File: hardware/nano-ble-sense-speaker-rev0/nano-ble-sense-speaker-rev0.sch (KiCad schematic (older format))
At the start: 1 part, among them J1 Arduino-NANO-33

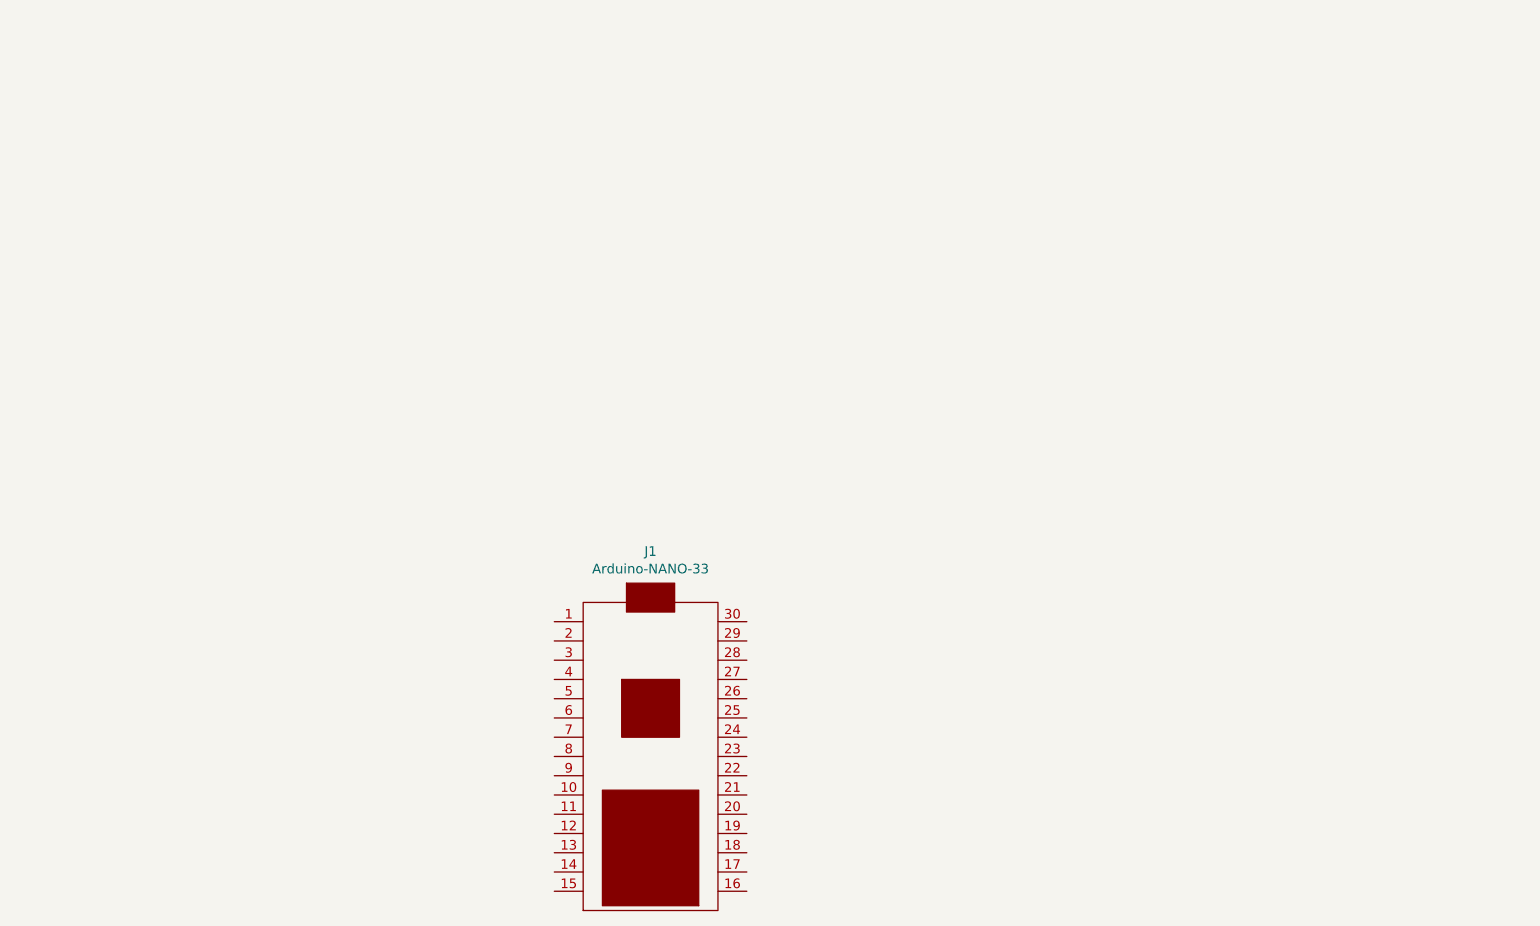
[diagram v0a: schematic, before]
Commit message: Make first PCB design
PCB Design in KiCAD now has:
- OLED 1.3inch
- power supply using LM7805 and capacitors

TODO:
- Add I2S module either as the breakout board of on the PCB as an SMD
comp.
- Move components a little more closer.
- Add PCB ground pad, and make paths between all components.
- Add pull up resistors to the OLED I2C pins

Signed-off-by: Dhruva Gole <goledhruva@gmail.com>
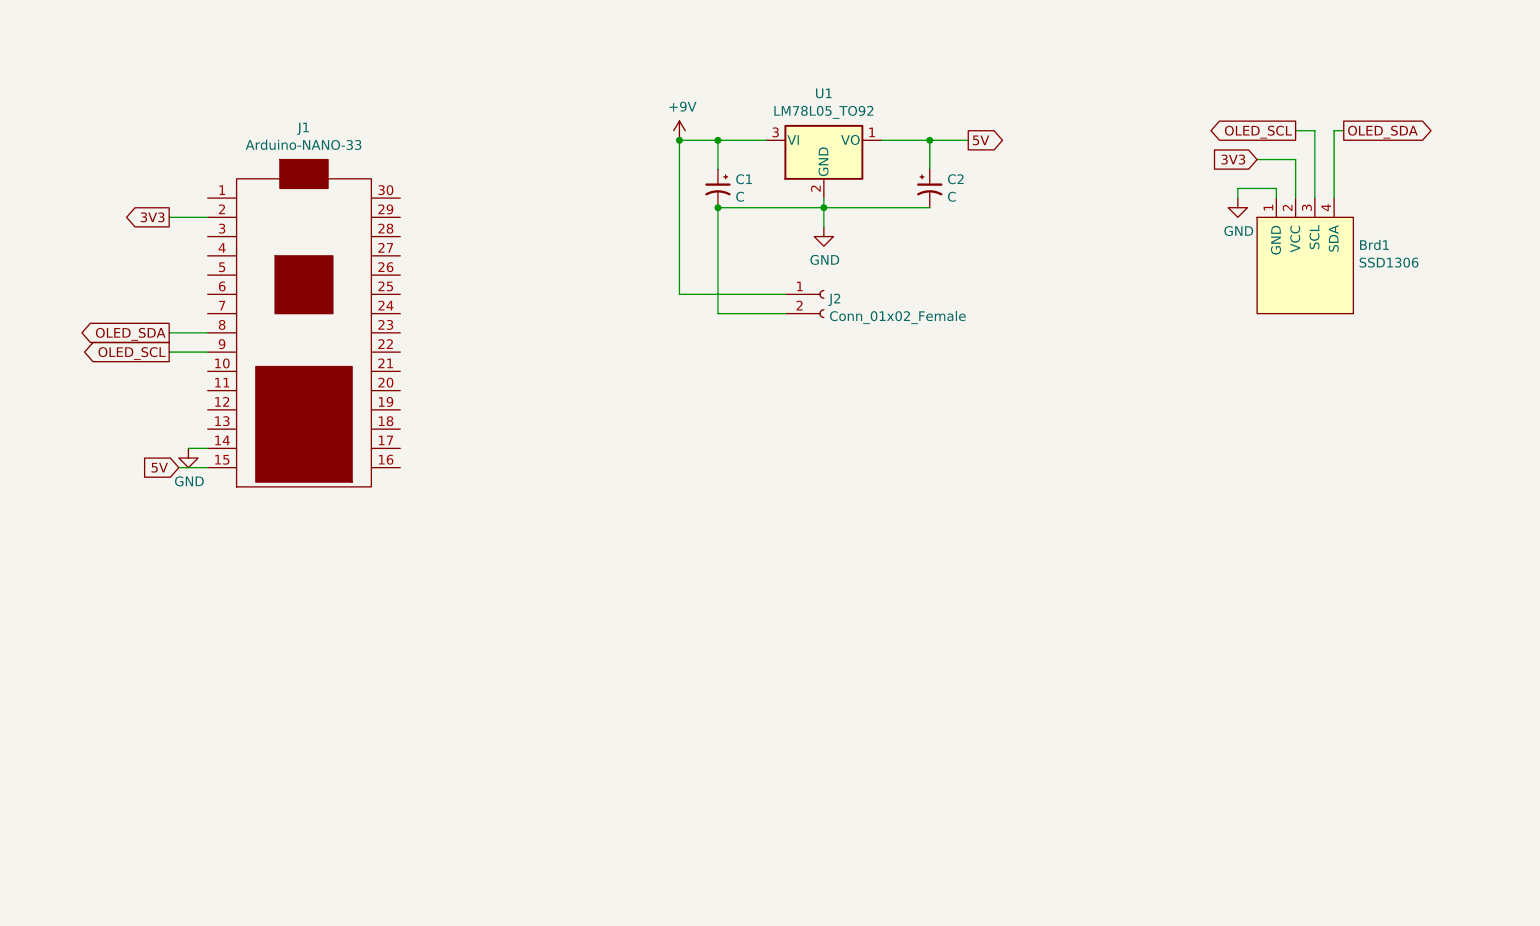
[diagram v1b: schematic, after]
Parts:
- added Brd1: SSD1306, SSD1306:128x64OLED, symbol SSD1306-128x64_OLED:SSD1306
- added C1, C2: C, Capacitor_THT:CP_Radial_D6.3mm_P2.50mm, symbol Device:CP1_Small
- added J2: Conn_01x02_Female, Connector_PinSocket_2.54mm:PinSocket_1x02_P2.54mm_Vertical, symbol Connector:Conn_01x02_Female
- added U1: LM78L05_TO92, Package_TO_SOT_THT:TO-220-3_Vertical, symbol Linear-reg:LM78L05_TO92
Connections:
- net GND: now reaches J1.14
- net GND: now also Brd1.1 (GND), C1.2, C2.2, J2.2 (Pin_2), U1.2 (GND)
- net 5V: now reaches J1.15
- net 5V: now also C2.1, U1.1 (VO)
- net 3V3: now reaches J1.2
- net 3V3: now also Brd1.2 (VCC)
- net OLED_SDA: now reaches J1.8
- net OLED_SDA: now also Brd1.4 (SDA)
- net OLED_SCL: now reaches J1.9
- net OLED_SCL: now also Brd1.3 (SCL)
- new net +9V: C1.1, J2.1 (Pin_1), U1.3 (VI)
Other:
- moved on the sheet: J1
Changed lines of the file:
@@
 L Arduino-nano-33:Arduino-NANO-33 J1
 U 1 1 6140B0DA
-P 3850 4300
-F 0 "J1" H 3850 5365 50  0000 C CNN
-F 1 "Arduino-NANO-33" H 3850 5274 50  0000 C CNN
-F 2 "Nano_33:NANO_33_Socket_Castell" H 3525 4200 50  0001 C CNN
-F 3 "~" H 3525 4200 50  0001 C CNN
-	1    3850 4300
+P 2050 2100
+F 0 "J1" H 2050 3165 50  0000 C CNN
+F 1 "Arduino-NANO-33" H 2050 3074 50  0000 C CNN
+F 2 "Nano_33:NANO_33_Socket_Castell" H 1725 2000 50  0001 C CNN
+F 3 "~" H 1725 2000 50  0001 C CNN
+	1    2050 2100
 	1    0    0    -1
 $EndComp
+Text GLabel 1400 2800 0    50   Input ~ 0
+5V
+Wire Wire Line
+	1400 2800 1550 2800
+Text GLabel 5500 1100 2    50   Output ~ 0
+5V
+$Comp
+L power:GND #PWR0101
+U 1 1 616D7A98
+P 4750 1550
+F 0 "#PWR0101" H 4750 1300 50  0001 C CNN
+F 1 "GND" H 4755 1377 50  0000 C CNN
+F 2 "" H 4750 1550 50  0001 C CNN
+F 3 "" H 4750 1550 50  0001 C CNN
+	1    4750 1550
+	1    0    0    -1
+$EndComp
+$Comp
+L power:GND #PWR0102
+U 1 1 616D7EA0
+P 1450 2700
+F 0 "#PWR0102" H 1450 2450 50  0001 C CNN
+F 1 "GND" H 1455 2527 50  0000 C CNN
+F 2 "" H 1450 2700 50  0001 C CNN
+F 3 "" H 1450 2700 50  0001 C CNN
+	1    1450 2700
+	1    0    0    -1
+$EndComp
+Wire Wire Line
+	1450 2700 1550 2700
+Wire Wire Line
+	4750 1400 4750 1450
+$Comp
+L Linear-reg:LM78L05_TO92 U1
+U 1 1 616D28C0
+P 4750 1100
+F 0 "U1" H 4750 1342 50  0000 C CNN
+F 1 "LM78L05_TO92" H 4750 1251 50  0000 C CNN
+F 2 "Package_TO_SOT_THT:TO-220-3_Vertical" H 4750 1325 50  0001 C CIN
+F 3 "https://www.onsemi.com/pub/Collateral/MC78L06A-D.pdf" H 4750 1050 50  0001 C CNN
+	1    4750 1100
+	1    0    0    -1
+$EndComp
+$Comp
+L Device:CP1_Small C2
+U 1 1 616F6CCF
+P 5300 1350
+F 0 "C2" H 5391 1396 50  0000 L CNN
+F 1 "C" H 5391 1305 50  0000 L CNN
+F 2 "Capacitor_THT:CP_Radial_D6.3mm_P2.50mm" H 5300 1350 50  0001 C CNN
+F 3 "~" H 5300 1350 50  0001 C CNN
+	1    5300 1350
+	1    0    0    -1
+$EndComp
+$Comp
+L Device:CP1_Small C1
+U 1 1 616FACC5
+P 4200 1350
+F 0 "C1" H 4109 1396 50  0000 R CNN
+F 1 "C" H 4109 1305 50  0000 R CNN
+F 2 "Capacitor_THT:CP_Radial_D6.3mm_P2.50mm" H 4200 1350 50  0001 C CNN
+F 3 "~" H 4200 1350 50  0001 C CNN
+	1    4200 1350
+	-1   0    0    -1
+$EndComp
+Wire Wire Line
+	5050 1100 5300 1100
+Wire Wire Line
+	5300 1250 5300 1100
+Connection ~ 5300 1100
+Wire Wire Line
+	5300 1100 5500 1100
+Wire Wire Line
+	4200 1250 4200 1100
+Wire Wire Line
+	4200 1100 4450 1100
+Wire Wire Line
+	4200 1450 4750 1450
+Connection ~ 4750 1450
+Wire Wire Line
+	4750 1450 4750 1550
+Wire Wire Line
+	5300 1450 4750 1450
+$Comp
+L power:+9V #PWR0103
+U 1 1 61703537
+P 4000 1100
+F 0 "#PWR0103" H 4000 950 50  0001 C CNN
+F 1 "+9V" H 4015 1273 50  0000 C CNN
+F 2 "" H 4000 1100 50  0001 C CNN
+F 3 "" H 4000 1100 50  0001 C CNN
+	1    4000 1100
+	1    0    0    -1
+$EndComp
+Wire Wire Line
+	4000 1100 4200 1100
+Connection ~ 4200 1100
+$Comp
+L Connector:Conn_01x02_Female J2
+U 1 1 6170C5E3
+P 4750 1900
+F 0 "J2" H 4778 1876 50  0000 L CNN
+F 1 "Conn_01x02_Female" H 4778 1785 50  0000 L CNN
+F 2 "Connector_PinSocket_2.54mm:PinSocket_1x02_P2.54mm_Vertical" H 4750 1900 50  0001 C CNN
+F 3 "~" H 4750 1900 50  0001 C CNN
+	1    4750 1900
+	1    0    0    -1
+$EndComp
+Wire Wire Line
+	4000 1100 4000 1900
+Wire Wire Line
+	4000 1900 4550 1900
+Connection ~ 4000 1100
+Wire Wire Line
+	4200 1450 4200 2000
+Wire Wire Line
+	4200 2000 4550 2000
+Connection ~ 4200 1450
+$Comp
+L SSD1306-128x64_OLED:SSD1306 Brd1
+U 1 1 61713D71
+P 7250 1750
+F 0 "Brd1" H 7528 1854 50  0000 L CNN
+F 1 "SSD1306" H 7528 1763 50  0000 L CNN
+F 2 "SSD1306:128x64OLED" H 7250 2000 50  0001 C CNN
+F 3 "" H 7250 2000 50  0001 C CNN
+	1    7250 1750
+	1    0    0    -1
+$EndComp
+Text GLabel 1350 1500 0    50   Output ~ 0
+3V3
+Text GLabel 7000 1200 0    50   Input ~ 0
+3V3
+$Comp
+L power:GND #PWR0104
+U 1 1 61718B31
+P 6900 1400
+F 0 "#PWR0104" H 6900 1150 50  0001 C CNN
+F 1 "GND" H 6905 1227 50  0000 C CNN
+F 2 "" H 6900 1400 50  0001 C CNN
+F 3 "" H 6900 1400 50  0001 C CNN
+	1    6900 1400
+	1    0    0    -1
+$EndComp
+Wire Wire Line
+	6900 1400 6900 1350
+Wire Wire Line
+	6900 1350 7100 1350
+Wire Wire Line
+	7100 1350 7100 1400
+Wire Wire Line
+	7200 1200 7200 1400
+Wire Wire Line
+	7200 1200 7000 1200
+Text GLabel 7200 1050 0    50   Output ~ 0
+OLED_SCL
+Text GLabel 7450 1050 2    50   Output ~ 0
+OLED_SDA
+Wire Wire Line
+	7200 1050 7300 1050
+Wire Wire Line
+	7300 1050 7300 1400
+Wire Wire Line
+	7400 1400 7400 1050
+Wire Wire Line
+	7400 1050 7450 1050
+Text GLabel 1350 2100 0    50   Output ~ 0
+OLED_SDA
+Text GLabel 1350 2200 0    50   Output ~ 0
+OLED_SCL
+Wire Wire Line
+	1350 2100 1550 2100
+Wire Wire Line
+	1350 2200 1550 2200
+Wire Wire Line
+	1350 1500 1550 1500
 $EndSCHEMATC

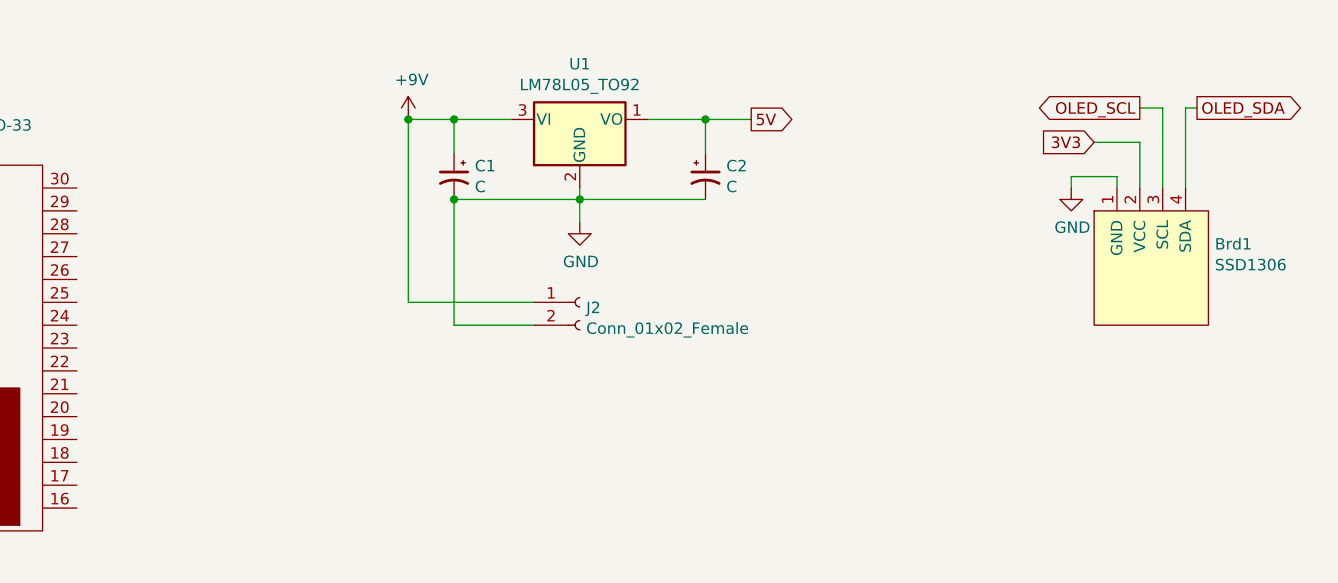
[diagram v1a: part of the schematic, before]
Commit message: Add pull up resistors to I2C
Signed-off-by: Dhruva Gole <goledhruva@gmail.com>
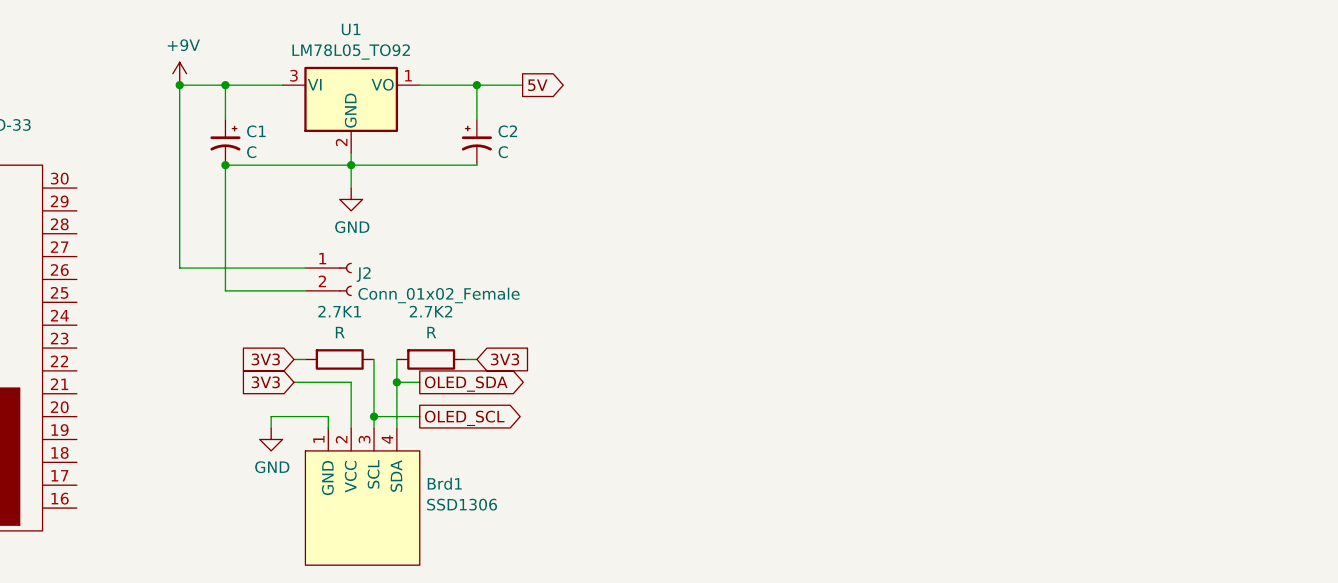
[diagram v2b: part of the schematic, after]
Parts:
- added 2.7K1, 2.7K2: R, Resistor_SMD:R_0603_1608Metric_Pad0.98x0.95mm_HandSolder, symbol Device:R
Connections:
- net 3V3: now also 2.7K1.2, 2.7K2.1
- net OLED_SCL: now also 2.7K1.1
- net OLED_SDA: now also 2.7K2.2
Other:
- moved on the sheet: Brd1, C1, C2, J2, U1
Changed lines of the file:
@@
 Wire Wire Line
 	1400 2800 1550 2800
-Text GLabel 5500 1100 2    50   Output ~ 0
+Text GLabel 4500 950  2    50   Output ~ 0
 5V
 $Comp
 L power:GND #PWR0101
 U 1 1 616D7A98
-P 4750 1550
-F 0 "#PWR0101" H 4750 1300 50  0001 C CNN
-F 1 "GND" H 4755 1377 50  0000 C CNN
-F 2 "" H 4750 1550 50  0001 C CNN
-F 3 "" H 4750 1550 50  0001 C CNN
-	1    4750 1550
+P 3750 1400
+F 0 "#PWR0101" H 3750 1150 50  0001 C CNN
+F 1 "GND" H 3755 1227 50  0000 C CNN
+F 2 "" H 3750 1400 50  0001 C CNN
+F 3 "" H 3750 1400 50  0001 C CNN
+	1    3750 1400
 	1    0    0    -1
 $EndComp
@@
 	1450 2700 1550 2700
 Wire Wire Line
-	4750 1400 4750 1450
+	3750 1250 3750 1300
 $Comp
 L Linear-reg:LM78L05_TO92 U1
 U 1 1 616D28C0
-P 4750 1100
-F 0 "U1" H 4750 1342 50  0000 C CNN
-F 1 "LM78L05_TO92" H 4750 1251 50  0000 C CNN
-F 2 "Package_TO_SOT_THT:TO-220-3_Vertical" H 4750 1325 50  0001 C CIN
-F 3 "https://www.onsemi.com/pub/Collateral/MC78L06A-D.pdf" H 4750 1050 50  0001 C CNN
-	1    4750 1100
+P 3750 950
+F 0 "U1" H 3750 1192 50  0000 C CNN
+F 1 "LM78L05_TO92" H 3750 1101 50  0000 C CNN
+F 2 "Package_TO_SOT_THT:TO-220-3_Vertical" H 3750 1175 50  0001 C CIN
+F 3 "https://www.onsemi.com/pub/Collateral/MC78L06A-D.pdf" H 3750 900 50  0001 C CNN
+	1    3750 950
 	1    0    0    -1
 $EndComp
@@
 L Device:CP1_Small C2
 U 1 1 616F6CCF
-P 5300 1350
-F 0 "C2" H 5391 1396 50  0000 L CNN
-F 1 "C" H 5391 1305 50  0000 L CNN
-F 2 "Capacitor_THT:CP_Radial_D6.3mm_P2.50mm" H 5300 1350 50  0001 C CNN
-F 3 "~" H 5300 1350 50  0001 C CNN
-	1    5300 1350
+P 4300 1200
+F 0 "C2" H 4391 1246 50  0000 L CNN
+F 1 "C" H 4391 1155 50  0000 L CNN
+F 2 "Capacitor_THT:CP_Radial_D6.3mm_P2.50mm" H 4300 1200 50  0001 C CNN
+F 3 "~" H 4300 1200 50  0001 C CNN
+	1    4300 1200
 	1    0    0    -1
 $EndComp
@@
 L Device:CP1_Small C1
 U 1 1 616FACC5
-P 4200 1350
-F 0 "C1" H 4109 1396 50  0000 R CNN
-F 1 "C" H 4109 1305 50  0000 R CNN
-F 2 "Capacitor_THT:CP_Radial_D6.3mm_P2.50mm" H 4200 1350 50  0001 C CNN
-F 3 "~" H 4200 1350 50  0001 C CNN
-	1    4200 1350
+P 3200 1200
+F 0 "C1" H 3109 1246 50  0000 R CNN
+F 1 "C" H 3109 1155 50  0000 R CNN
+F 2 "Capacitor_THT:CP_Radial_D6.3mm_P2.50mm" H 3200 1200 50  0001 C CNN
+F 3 "~" H 3200 1200 50  0001 C CNN
+	1    3200 1200
 	-1   0    0    -1
 $EndComp
 Wire Wire Line
-	5050 1100 5300 1100
-Wire Wire Line
-	5300 1250 5300 1100
-Connection ~ 5300 1100
-Wire Wire Line
-	5300 1100 5500 1100
-Wire Wire Line
-	4200 1250 4200 1100
-Wire Wire Line
-	4200 1100 4450 1100
-Wire Wire Line
-	4200 1450 4750 1450
-Connection ~ 4750 1450
-Wire Wire Line
-	4750 1450 4750 1550
-Wire Wire Line
-	5300 1450 4750 1450
+	4050 950  4300 950
+Wire Wire Line
+	4300 1100 4300 950
+Connection ~ 4300 950
+Wire Wire Line
+	4300 950  4500 950
+Wire Wire Line
+	3200 1100 3200 950
+Wire Wire Line
+	3200 950  3450 950
+Wire Wire Line
+	3200 1300 3750 1300
+Connection ~ 3750 1300
+Wire Wire Line
+	3750 1300 3750 1400
+Wire Wire Line
+	4300 1300 3750 1300
 $Comp
 L power:+9V #PWR0103
 U 1 1 61703537
-P 4000 1100
-F 0 "#PWR0103" H 4000 950 50  0001 C CNN
-F 1 "+9V" H 4015 1273 50  0000 C CNN
-F 2 "" H 4000 1100 50  0001 C CNN
-F 3 "" H 4000 1100 50  0001 C CNN
-	1    4000 1100
-	1    0    0    -1
-$EndComp
-Wire Wire Line
-	4000 1100 4200 1100
-Connection ~ 4200 1100
+P 3000 950
+F 0 "#PWR0103" H 3000 800 50  0001 C CNN
+F 1 "+9V" H 3015 1123 50  0000 C CNN
+F 2 "" H 3000 950 50  0001 C CNN
+F 3 "" H 3000 950 50  0001 C CNN
+	1    3000 950
+	1    0    0    -1
+$EndComp
+Wire Wire Line
+	3000 950  3200 950
+Connection ~ 3200 950
 $Comp
 L Connector:Conn_01x02_Female J2
 U 1 1 6170C5E3
-P 4750 1900
-F 0 "J2" H 4778 1876 50  0000 L CNN
-F 1 "Conn_01x02_Female" H 4778 1785 50  0000 L CNN
-F 2 "Connector_PinSocket_2.54mm:PinSocket_1x02_P2.54mm_Vertical" H 4750 1900 50  0001 C CNN
-F 3 "~" H 4750 1900 50  0001 C CNN
-	1    4750 1900
-	1    0    0    -1
-$EndComp
-Wire Wire Line
-	4000 1100 4000 1900
-Wire Wire Line
-	4000 1900 4550 1900
-Connection ~ 4000 1100
-Wire Wire Line
-	4200 1450 4200 2000
-Wire Wire Line
-	4200 2000 4550 2000
-Connection ~ 4200 1450
+P 3750 1750
+F 0 "J2" H 3778 1726 50  0000 L CNN
+F 1 "Conn_01x02_Female" H 3778 1635 50  0000 L CNN
+F 2 "Connector_PinSocket_2.54mm:PinSocket_1x02_P2.54mm_Vertical" H 3750 1750 50  0001 C CNN
+F 3 "~" H 3750 1750 50  0001 C CNN
+	1    3750 1750
+	1    0    0    -1
+$EndComp
+Wire Wire Line
+	3000 950  3000 1750
+Wire Wire Line
+	3000 1750 3550 1750
+Connection ~ 3000 950
+Wire Wire Line
+	3200 1300 3200 1850
+Wire Wire Line
+	3200 1850 3550 1850
+Connection ~ 3200 1300
 $Comp
 L SSD1306-128x64_OLED:SSD1306 Brd1
 U 1 1 61713D71
-P 7250 1750
-F 0 "Brd1" H 7528 1854 50  0000 L CNN
-F 1 "SSD1306" H 7528 1763 50  0000 L CNN
-F 2 "SSD1306:128x64OLED" H 7250 2000 50  0001 C CNN
-F 3 "" H 7250 2000 50  0001 C CNN
-	1    7250 1750
+P 3800 2800
+F 0 "Brd1" H 4078 2904 50  0000 L CNN
+F 1 "SSD1306" H 4078 2813 50  0000 L CNN
+F 2 "SSD1306:128x64OLED" H 3800 3050 50  0001 C CNN
+F 3 "" H 3800 3050 50  0001 C CNN
+	1    3800 2800
 	1    0    0    -1
 $EndComp
 Text GLabel 1350 1500 0    50   Output ~ 0
 3V3
-Text GLabel 7000 1200 0    50   Input ~ 0
+Text GLabel 3500 2250 0    50   Input ~ 0
 3V3
 $Comp
 L power:GND #PWR0104
 U 1 1 61718B31
-P 6900 1400
-F 0 "#PWR0104" H 6900 1150 50  0001 C CNN
-F 1 "GND" H 6905 1227 50  0000 C CNN
-F 2 "" H 6900 1400 50  0001 C CNN
-F 3 "" H 6900 1400 50  0001 C CNN
-	1    6900 1400
-	1    0    0    -1
-$EndComp
-Wire Wire Line
-	6900 1400 6900 1350
-Wire Wire Line
-	6900 1350 7100 1350
-Wire Wire Line
-	7100 1350 7100 1400
-Wire Wire Line
-	7200 1200 7200 1400
-Wire Wire Line
-	7200 1200 7000 1200
-Text GLabel 7200 1050 0    50   Output ~ 0
+P 3400 2450
+F 0 "#PWR0104" H 3400 2200 50  0001 C CNN
+F 1 "GND" H 3405 2277 50  0000 C CNN
+F 2 "" H 3400 2450 50  0001 C CNN
+F 3 "" H 3400 2450 50  0001 C CNN
+	1    3400 2450
+	1    0    0    -1
+$EndComp
+Wire Wire Line
+	3650 2400 3650 2450
+Wire Wire Line
+	3750 2250 3750 2450
+Text GLabel 4050 2400 2    50   Output ~ 0
 OLED_SCL
-Text GLabel 7450 1050 2    50   Output ~ 0
+Text GLabel 4050 2250 2    50   Output ~ 0
 OLED_SDA
-Wire Wire Line
-	7200 1050 7300 1050
-Wire Wire Line
-	7300 1050 7300 1400
-Wire Wire Line
-	7400 1400 7400 1050
-Wire Wire Line
-	7400 1050 7450 1050
 Text GLabel 1350 2100 0    50   Output ~ 0
 OLED_SDA
@@
 Wire Wire Line
 	1350 1500 1550 1500
+$Comp
+L Device:R 2.7K2
+U 1 1 616C6DBD
+P 4100 2150
+F 0 "2.7K2" V 3893 2150 50  0000 C CNN
+F 1 "R" V 3984 2150 50  0000 C CNN
+F 2 "Resistor_SMD:R_0603_1608Metric_Pad0.98x0.95mm_HandSolder" V 4030 2150 50  0001 C CNN
+F 3 "~" H 4100 2150 50  0001 C CNN
+	1    4100 2150
+	0    1    1    0
+$EndComp
+$Comp
+L Device:R 2.7K1
+U 1 1 616C707B
+P 3700 2150
+F 0 "2.7K1" V 3493 2150 50  0000 C CNN
+F 1 "R" V 3584 2150 50  0000 C CNN
+F 2 "Resistor_SMD:R_0603_1608Metric_Pad0.98x0.95mm_HandSolder" V 3630 2150 50  0001 C CNN
+F 3 "~" H 3700 2150 50  0001 C CNN
+	1    3700 2150
+	0    1    1    0
+$EndComp
+Text GLabel 4300 2150 2    50   Input ~ 0
+3V3
+Text GLabel 3500 2150 0    50   Input ~ 0
+3V3
+Wire Wire Line
+	3400 2400 3400 2450
+Wire Wire Line
+	3400 2400 3650 2400
+Wire Wire Line
+	3500 2250 3750 2250
+Wire Wire Line
+	3500 2150 3550 2150
+Wire Wire Line
+	3850 2450 3850 2400
+Wire Wire Line
+	4050 2250 3950 2250
+Wire Wire Line
+	4050 2400 3850 2400
+Connection ~ 3850 2400
+Wire Wire Line
+	3850 2400 3850 2150
+Wire Wire Line
+	3950 2450 3950 2250
+Wire Wire Line
+	4250 2150 4300 2150
+Wire Wire Line
+	3950 2150 3950 2250
+Connection ~ 3950 2250
 $EndSCHEMATC
